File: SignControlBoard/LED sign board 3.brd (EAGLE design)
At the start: 69.5 x 55.9 mm, 45 parts, among them IC1 MSGEQ7DIL, U1 ATMEGA328P, U2 M5205 5v, Y1 16MHz

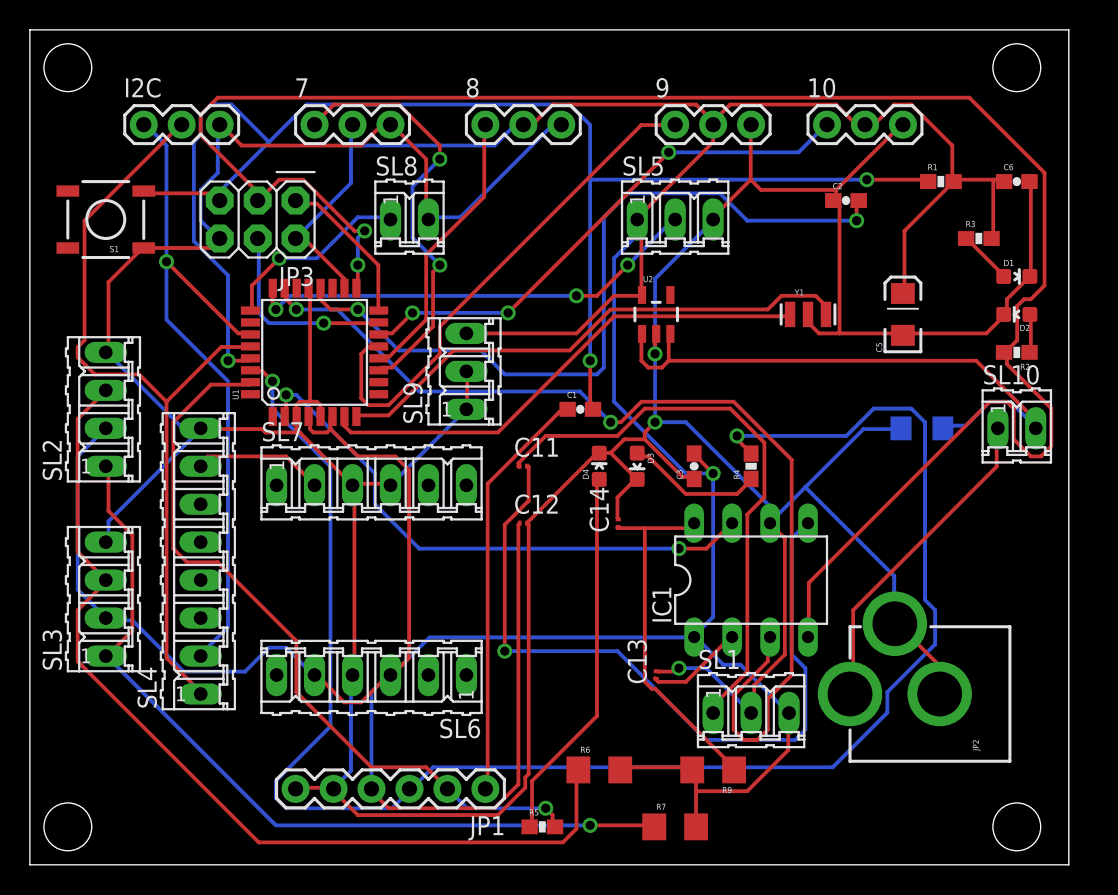
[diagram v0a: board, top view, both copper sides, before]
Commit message: Updated LED Boards
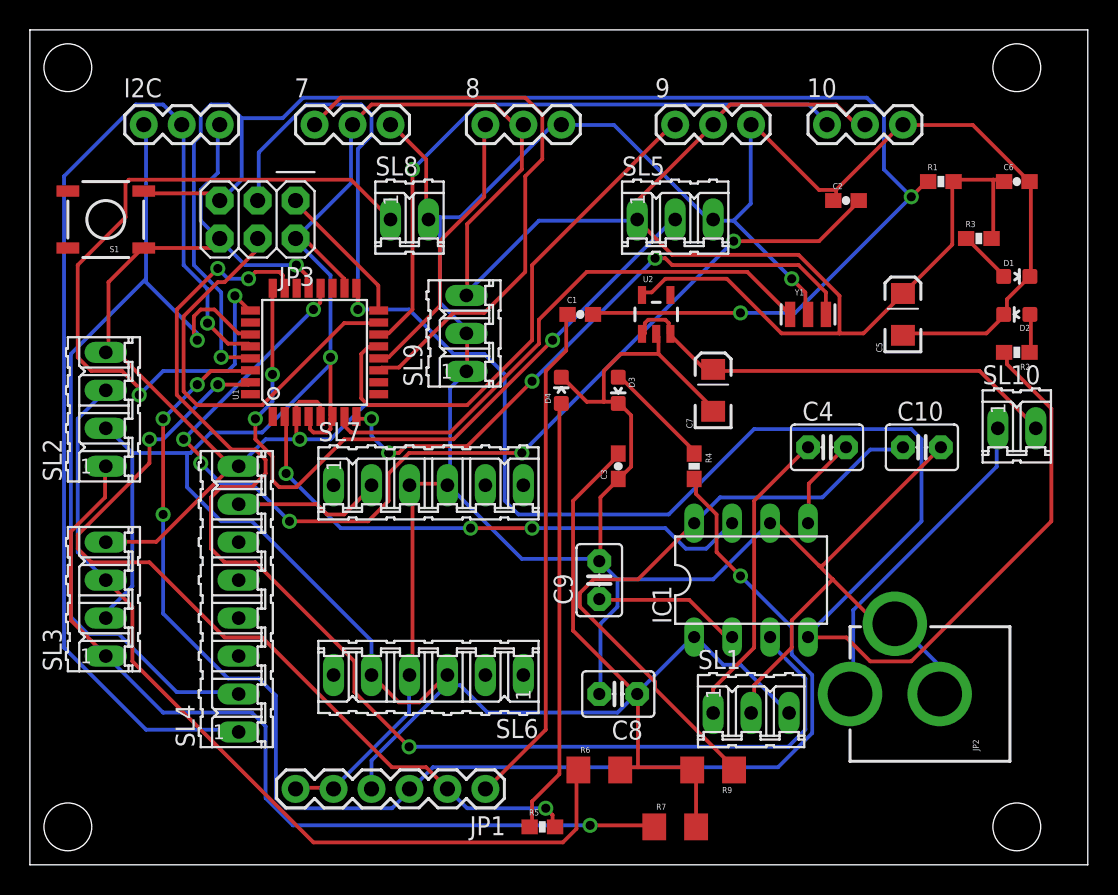
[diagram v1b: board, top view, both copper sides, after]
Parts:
- removed C11: 0.01uf, eagle-ltspice:C0201
- removed C12, C13: 0.1uf, eagle-ltspice:C0201
- removed C14: 33pf, eagle-ltspice:C0201
- added C10: 33pf, capacitor-wima:C2.5-3
- added C7: 10uF, SparkFun-Passives:EIA3216
- added C8, C9: 0.1uf, capacitor-wima:C2.5-3
- C4: value 10uF -> 0.01uf; device SparkFun-Passives:EIA3216 -> capacitor-wima:C2.5-3
- moved C4 6.48 mm to (53.3, 26.7), flipped to the top, turned to 0 degrees
- moved C1 6.35 mm to (36.8, 35.6)
- moved D4 5.68 mm to (35.6, 30.5)
- moved D3 5.24 mm to (39.4, 30.5)
- moved C3 5.08 mm to (39.4, 25.4)
- moved SL6 3.81 mm to (26.7, 11.4)
- moved SL7 3.81 mm to (26.7, 24.1)
- moved R4 3.81 mm to (44.5, 25.4), turned to 270 degrees
- moved SL4 3.59 mm to (14.0, 16.5)
- moved SL9 2.54 mm to (29.2, 34.3)
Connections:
- net GND: now also C10.2, C7.C, C8.2, C9.2; no longer C12.2, C13.2, C14.2, C4.C
- net N$10: now also C4.2; no longer C11.2
- net N$11: now also C9.1; no longer C13.1
- net N$12: now also C10.1; no longer C14.1
- net N$9: now also C4.1; no longer C11.1
- net VCC: now also C8.1; no longer C12.1
- net VIN: now also C7.A; no longer C4.A
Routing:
- net N$10: track 50.7 -> 6.14 mm, vias 1 -> 0
- net A2: track 13.0 -> 50.6 mm, vias 1 -> 2
- net SCL: track 53.3 -> 73.7 mm, vias 0 -> 1
- net AREF: track 51.8 -> 71.6 mm, vias 2 -> 6
- net N$9: track 38.7 -> 20.4 mm
- net A1: track 30.7 -> 48.3 mm
- net N$12: track 24.1 -> 41.8 mm
- net RXI: track 113.0 -> 95.5 mm, vias 2 -> 4
- net A0: track 69.1 -> 86.0 mm, vias 2 -> 3
- net MOSI: track 13.3 -> 28.3 mm, vias 1 -> 0
- net SDA: track 46.3 -> 60.5 mm
- net VCC: track 286.4 -> 274.3 mm
- net D7: track 28.8 -> 40.0 mm, vias 2 -> 0
- net RESET: track 100.6 -> 110.4 mm
- net VIN: track 40.3 -> 30.7 mm
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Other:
- board size 69.5 x 55.9 mm -> 70.8 x 55.9 mm
